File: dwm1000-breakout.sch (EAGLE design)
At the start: 11 parts, among them U2 DWM1000

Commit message: Rand's nitpicking
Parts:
- removed C1: 0.1uF, rcl:C-USC1206
- added C2: (no value), Passives:CAPACITOR_NP_1210
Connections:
- net +3V3: now also C2.P$1; no longer C1.1
- net GND: now also C2.P$2; no longer C1.2, RX.C, TX.C
- net N$1: now also R1.2, RX.C; no longer R1.1, RX.A
- net N$2: now also R2.2, TX.C; no longer R2.1, TX.A
- net RXLED: now also RX.A; no longer R1.2
- net TXLED: now also TX.A; no longer R2.2
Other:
- moved on the sheet: R1, R2, RX, TX
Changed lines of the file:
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@@
 <part name="SV1" library="con-lstb" library_urn="urn:adsk.eagle:library:162" deviceset="MA07-1" device=""/>
 <part name="SV2" library="con-lstb" library_urn="urn:adsk.eagle:library:162" deviceset="MA07-1" device=""/>
-<part name="C1" library="rcl" library_urn="urn:adsk.eagle:library:334" deviceset="C-US" device="C1206" value="0.1uF"/>
 <part name="R1" library="rcl" library_urn="urn:adsk.eagle:library:334" deviceset="R-US_" device="R1206" value="470"/>
 <part name="R2" library="rcl" library_urn="urn:adsk.eagle:library:334" deviceset="R-US_" device="R1206" value="470"/>
@@
 <part name="PWR" library="led" library_urn="urn:adsk.eagle:library:259" deviceset="LED" device="SMT1206"/>
 <part name="R4" library="rcl" library_urn="urn:adsk.eagle:library:334" deviceset="R-US_" device="R1206"/>
+<part name="C2" library="Passives" deviceset="CAPACITOR_NP" device="_1210"/>
 </parts>
 <sheets>
@@
 <attribute name="VALUE" x="123.19" y="22.86" size="1.778" layer="96"/>
 </instance>
-<instance part="C1" gate="G$1" x="210.82" y="38.1"/>
-<instance part="R1" gate="G$1" x="180.34" y="35.56" rot="R180"/>
-<instance part="R2" gate="G$1" x="180.34" y="43.18" rot="R180"/>
+<instance part="R1" gate="G$1" x="193.04" y="35.56" rot="R180"/>
+<instance part="R2" gate="G$1" x="193.04" y="43.18" rot="R180"/>
 <instance part="R3" gate="G$1" x="180.34" y="27.94" rot="R180"/>
-<instance part="RX" gate="G$1" x="190.5" y="35.56" rot="R90"/>
-<instance part="TX" gate="G$1" x="190.5" y="43.18" rot="R90"/>
+<instance part="RX" gate="G$1" x="175.26" y="35.56" rot="R90"/>
+<instance part="TX" gate="G$1" x="180.34" y="43.18" rot="R90"/>
 <instance part="SUPPLY1" gate="GND" x="200.66" y="15.24"/>
 <instance part="+3V1" gate="G$1" x="210.82" y="48.26"/>
 <instance part="PWR" gate="G$1" x="190.5" y="53.34" rot="R90"/>
 <instance part="R4" gate="G$1" x="180.34" y="53.34"/>
+<instance part="C2" gate="G$1" x="210.82" y="35.56"/>
 </instances>
 <busses>
@@
 </segment>
 <segment>
-<pinref part="TX" gate="G$1" pin="C"/>
-<wire x1="195.58" y1="43.18" x2="200.66" y2="43.18" width="0.1524" layer="91"/>
-<wire x1="200.66" y1="43.18" x2="200.66" y2="35.56" width="0.1524" layer="91"/>
 <pinref part="SUPPLY1" gate="GND" pin="GND"/>
-<pinref part="RX" gate="G$1" pin="C"/>
-<wire x1="200.66" y1="35.56" x2="200.66" y2="27.94" width="0.1524" layer="91"/>
 <wire x1="200.66" y1="27.94" x2="200.66" y2="17.78" width="0.1524" layer="91"/>
-<wire x1="195.58" y1="35.56" x2="200.66" y2="35.56" width="0.1524" layer="91"/>
-<junction x="200.66" y="35.56"/>
 <pinref part="R3" gate="G$1" pin="1"/>
 <wire x1="185.42" y1="27.94" x2="200.66" y2="27.94" width="0.1524" layer="91"/>
 <junction x="200.66" y="27.94"/>
-<pinref part="C1" gate="G$1" pin="2"/>
-<wire x1="210.82" y1="33.02" x2="210.82" y2="27.94" width="0.1524" layer="91"/>
 <wire x1="210.82" y1="27.94" x2="200.66" y2="27.94" width="0.1524" layer="91"/>
 <pinref part="PWR" gate="G$1" pin="C"/>
 <wire x1="195.58" y1="53.34" x2="200.66" y2="53.34" width="0.1524" layer="91"/>
-<wire x1="200.66" y1="53.34" x2="200.66" y2="43.18" width="0.1524" layer="91"/>
-<junction x="200.66" y="43.18"/>
+<wire x1="200.66" y1="53.34" x2="200.66" y2="27.94" width="0.1524" layer="91"/>
+<pinref part="C2" gate="G$1" pin="P$2"/>
+<wire x1="210.82" y1="27.94" x2="210.82" y2="30.48" width="0.1524" layer="91"/>
 </segment>
 </net>
@@
 </segment>
 <segment>
-<pinref part="C1" gate="G$1" pin="1"/>
-<wire x1="210.82" y1="40.64" x2="210.82" y2="45.72" width="0.1524" layer="91"/>
+<wire x1="210.82" y1="38.1" x2="210.82" y2="45.72" width="0.1524" layer="91"/>
 <pinref part="+3V1" gate="G$1" pin="+3V3"/>
+<pinref part="C2" gate="G$1" pin="P$1"/>
 </segment>
 <segment>
@@
 </segment>
 <segment>
-<pinref part="R2" gate="G$1" pin="2"/>
-<wire x1="175.26" y1="43.18" x2="170.18" y2="43.18" width="0.1524" layer="91"/>
 <label x="162.56" y="43.18" size="1.778" layer="95"/>
+<pinref part="TX" gate="G$1" pin="A"/>
+<wire x1="177.8" y1="43.18" x2="157.48" y2="43.18" width="0.1524" layer="91"/>
 </segment>
 </net>
@@
 </segment>
 <segment>
-<pinref part="R1" gate="G$1" pin="2"/>
-<wire x1="175.26" y1="35.56" x2="170.18" y2="35.56" width="0.1524" layer="91"/>
 <label x="162.56" y="35.56" size="1.778" layer="95"/>
+<pinref part="RX" gate="G$1" pin="A"/>
+<wire x1="172.72" y1="35.56" x2="170.18" y2="35.56" width="0.1524" layer="91"/>
 </segment>
 </net>
@@
 </segment>
 </net>
-<net name="N$1" class="0">
-<segment>
-<pinref part="R1" gate="G$1" pin="1"/>
-<pinref part="RX" gate="G$1" pin="A"/>
-<wire x1="185.42" y1="35.56" x2="187.96" y2="35.56" width="0.1524" layer="91"/>
-</segment>
-</net>
-<net name="N$2" class="0">
-<segment>
-<pinref part="R2" gate="G$1" pin="1"/>
-<pinref part="TX" gate="G$1" pin="A"/>
-<wire x1="185.42" y1="43.18" x2="187.96" y2="43.18" width="0.1524" layer="91"/>
-</segment>
-</net>
 <net name="N$3" class="0">
 <segment>
@@
 </segment>
 </net>
+<net name="N$1" class="0">
+<segment>
+<pinref part="RX" gate="G$1" pin="C"/>
+<pinref part="R1" gate="G$1" pin="2"/>
+<wire x1="180.34" y1="35.56" x2="187.96" y2="35.56" width="0.1524" layer="91"/>
+</segment>
+</net>
+<net name="N$2" class="0">
+<segment>
+<pinref part="TX" gate="G$1" pin="C"/>
+<pinref part="R2" gate="G$1" pin="2"/>
+<wire x1="185.42" y1="43.18" x2="187.96" y2="43.18" width="0.1524" layer="91"/>
+</segment>
+</net>

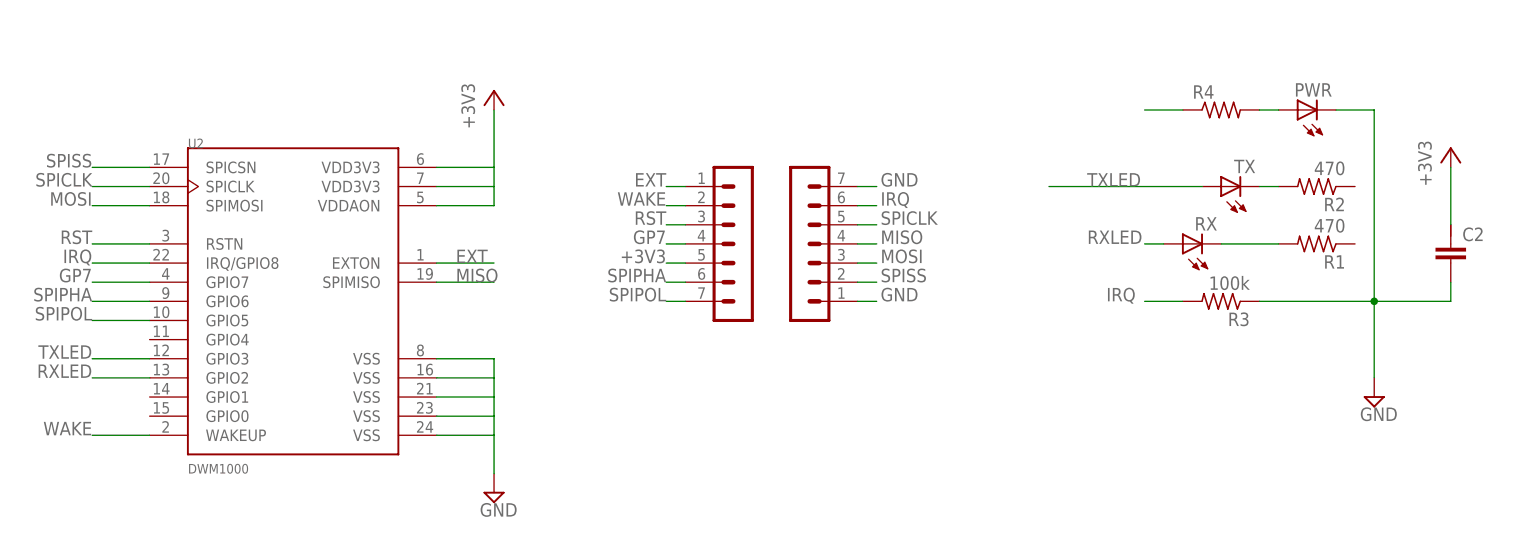
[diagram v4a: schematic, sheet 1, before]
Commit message: Whoops left some things unconnected. Fixed.
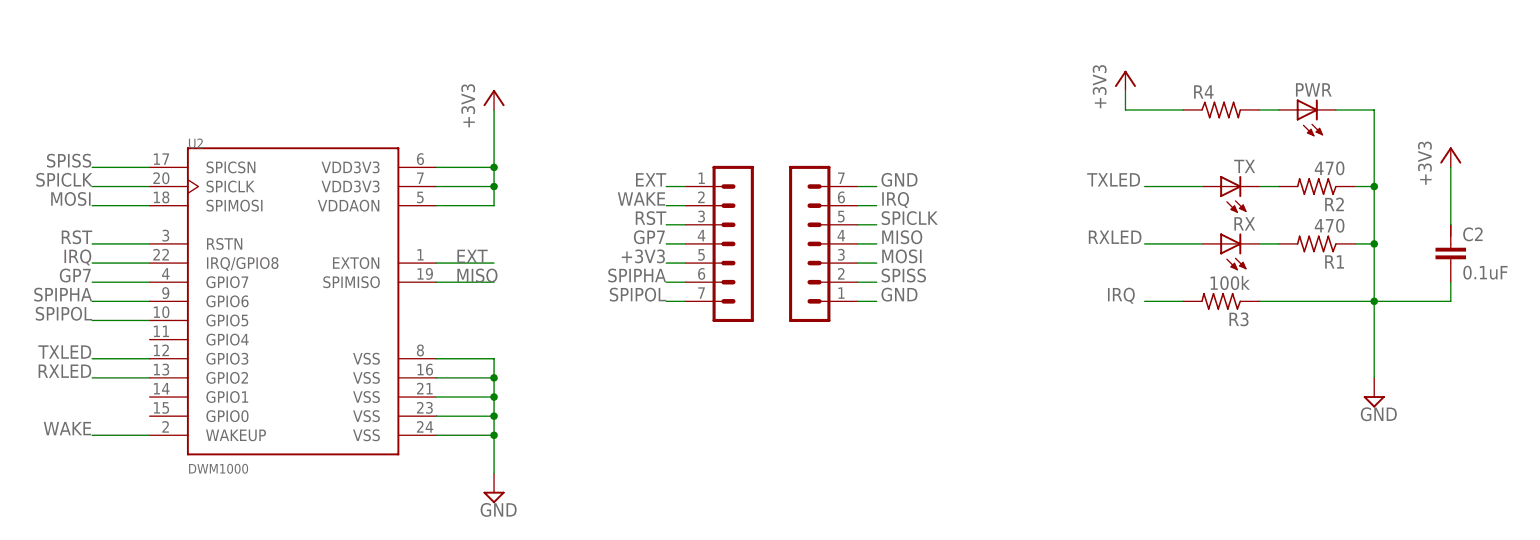
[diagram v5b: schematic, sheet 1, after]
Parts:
- C2: value (none) -> 0.1uF
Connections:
- net GND: now also R1.1, R2.1
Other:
- moved on the sheet: RX
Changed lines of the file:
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@@
 <part name="PWR" library="led" library_urn="urn:adsk.eagle:library:259" deviceset="LED" device="SMT1206"/>
 <part name="R4" library="rcl" library_urn="urn:adsk.eagle:library:334" deviceset="R-US_" device="R1206"/>
-<part name="C2" library="Passives" deviceset="CAPACITOR_NP" device="_1210"/>
+<part name="C2" library="Passives" deviceset="CAPACITOR_NP" device="_1210" value="0.1uF"/>
+<part name="+3V2" library="supply1" library_urn="urn:adsk.eagle:library:371" deviceset="+3V3" device=""/>
 </parts>
 <sheets>
@@
 <instance part="R2" gate="G$1" x="193.04" y="43.18" rot="R180"/>
 <instance part="R3" gate="G$1" x="180.34" y="27.94" rot="R180"/>
-<instance part="RX" gate="G$1" x="175.26" y="35.56" rot="R90"/>
+<instance part="RX" gate="G$1" x="180.34" y="35.56" rot="R90"/>
 <instance part="TX" gate="G$1" x="180.34" y="43.18" rot="R90"/>
 <instance part="SUPPLY1" gate="GND" x="200.66" y="15.24"/>
@@
 <instance part="R4" gate="G$1" x="180.34" y="53.34"/>
 <instance part="C2" gate="G$1" x="210.82" y="35.56"/>
+<instance part="+3V2" gate="G$1" x="167.64" y="58.42"/>
 </instances>
 <busses>
@@
 <wire x1="76.2" y1="10.16" x2="83.82" y2="10.16" width="0.1524" layer="91"/>
 <pinref part="SUPPLY4" gate="GND" pin="GND"/>
+<junction x="83.82" y="15.24"/>
+<junction x="83.82" y="12.7"/>
+<junction x="83.82" y="10.16"/>
+<junction x="83.82" y="17.78"/>
 </segment>
 <segment>
@@
 <pinref part="PWR" gate="G$1" pin="C"/>
 <wire x1="195.58" y1="53.34" x2="200.66" y2="53.34" width="0.1524" layer="91"/>
-<wire x1="200.66" y1="53.34" x2="200.66" y2="27.94" width="0.1524" layer="91"/>
+<wire x1="200.66" y1="53.34" x2="200.66" y2="43.18" width="0.1524" layer="91"/>
 <pinref part="C2" gate="G$1" pin="P$2"/>
+<wire x1="200.66" y1="43.18" x2="200.66" y2="35.56" width="0.1524" layer="91"/>
+<wire x1="200.66" y1="35.56" x2="200.66" y2="27.94" width="0.1524" layer="91"/>
 <wire x1="210.82" y1="27.94" x2="210.82" y2="30.48" width="0.1524" layer="91"/>
+<pinref part="R2" gate="G$1" pin="1"/>
+<wire x1="198.12" y1="43.18" x2="200.66" y2="43.18" width="0.1524" layer="91"/>
+<junction x="200.66" y="43.18"/>
+<pinref part="R1" gate="G$1" pin="1"/>
+<wire x1="198.12" y1="35.56" x2="200.66" y2="35.56" width="0.1524" layer="91"/>
+<junction x="200.66" y="35.56"/>
 </segment>
 </net>
@@
 <wire x1="76.2" y1="45.72" x2="83.82" y2="45.72" width="0.1524" layer="91"/>
 <pinref part="+3V3" gate="G$1" pin="+3V3"/>
+<junction x="83.82" y="45.72"/>
+<junction x="83.82" y="43.18"/>
 </segment>
 <segment>
@@
 <segment>
 <pinref part="R4" gate="G$1" pin="1"/>
-<wire x1="175.26" y1="53.34" x2="170.18" y2="53.34" width="0.1524" layer="91"/>
+<wire x1="175.26" y1="53.34" x2="167.64" y2="53.34" width="0.1524" layer="91"/>
+<pinref part="+3V2" gate="G$1" pin="+3V3"/>
+<wire x1="167.64" y1="53.34" x2="167.64" y2="55.88" width="0.1524" layer="91"/>
 </segment>
 </net>
@@
 <label x="162.56" y="43.18" size="1.778" layer="95"/>
 <pinref part="TX" gate="G$1" pin="A"/>
-<wire x1="177.8" y1="43.18" x2="157.48" y2="43.18" width="0.1524" layer="91"/>
+<wire x1="177.8" y1="43.18" x2="170.18" y2="43.18" width="0.1524" layer="91"/>
 </segment>
 </net>
@@
 <label x="162.56" y="35.56" size="1.778" layer="95"/>
 <pinref part="RX" gate="G$1" pin="A"/>
-<wire x1="172.72" y1="35.56" x2="170.18" y2="35.56" width="0.1524" layer="91"/>
+<wire x1="177.8" y1="35.56" x2="170.18" y2="35.56" width="0.1524" layer="91"/>
 </segment>
 </net>
@@
 <pinref part="RX" gate="G$1" pin="C"/>
 <pinref part="R1" gate="G$1" pin="2"/>
-<wire x1="180.34" y1="35.56" x2="187.96" y2="35.56" width="0.1524" layer="91"/>
-</segment>
-</net>
+<wire x1="185.42" y1="35.56" x2="187.96" y2="35.56" width="0.1524" layer="91"/>
+</segment>
+</net>

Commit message: Added part info
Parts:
- removed SV1, SV2: (no value), con-lstb:MA07-1
- added J1, J2: (no value), SparkFun-Connectors:CONN_07LOCK
- C2: DIGIKEY_PARTNUM (none) -> 1276-2854-1-ND
- PWR, RX: value (none) -> GREEN; device led:LEDSMT1206 -> SparkFun-LED:LED-GREEN1206; DIGIKEY_PARTNUM (none) -> 350-2053-1-ND
- R1, R2: value 470 -> 65; device rcl:R-US_R1206 -> SparkFun-Resistors:RESISTOR1206; DIGIKEY_PARTNUM (none) -> 311-64.9FRCT-ND
- R3: device rcl:R-US_R1206 -> SparkFun-Resistors:RESISTOR1206; DIGIKEY_PARTNUM (none) -> 311-100KERCT-ND
- R4: value (none) -> 65; device rcl:R-US_R1206 -> SparkFun-Resistors:RESISTOR1206; DIGIKEY_PARTNUM (none) -> 311-64.9FRCT-ND
- TX: value (none) -> GREEN; device led:LEDSMT1206 -> SparkFun-LED:LED-GREEN1206
- U2: DIGIKEY_PARTNUM (none) -> 1479-1002-1-ND
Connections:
- net +3V3: now also J2.3; no longer SV1.5
- net EXT: now also J2.7; no longer SV1.1
- net GND: now also J1.1, J1.7; no longer SV2.1, SV2.7
- net GP7: now also J2.4; no longer SV1.4
- net IRQ: now also J1.6; no longer SV2.6
- net MISO: now also J1.4; no longer SV2.4
- net MOSI: now also J1.3; no longer SV2.3
- net RST: now also J2.5; no longer SV1.3
- net SPICLK: now also J1.5; no longer SV2.5
- net SPIPHA: now also J2.2; no longer SV1.6
- net SPIPOL: now also J2.1; no longer SV1.7
- net SPISS: now also J1.2; no longer SV2.2
- net WAKE: now also J2.6; no longer SV1.2
